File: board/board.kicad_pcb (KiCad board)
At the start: 2 copper layers, 21 x 13 mm, 16 parts, among them J1 013_PoE_rectified, J2 014_PoE_controlled, Q1 PSMN5R2-60YL, U1 LT4275AIDDPBF-LT4275AIDDPBF

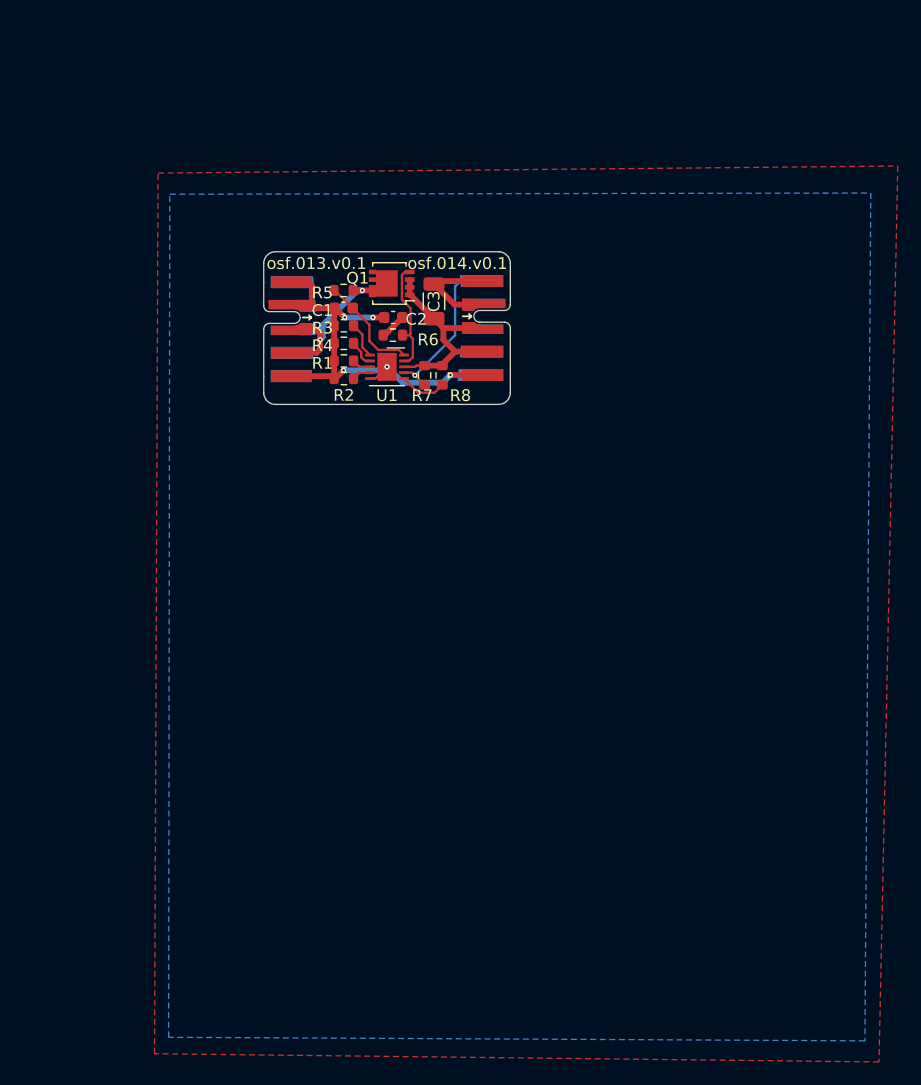
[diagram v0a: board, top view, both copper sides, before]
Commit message: changed PSMN5R2 footprint from LFPAK33 to LFPAK56
The PSMN5R2 is not available in LFPAK33.
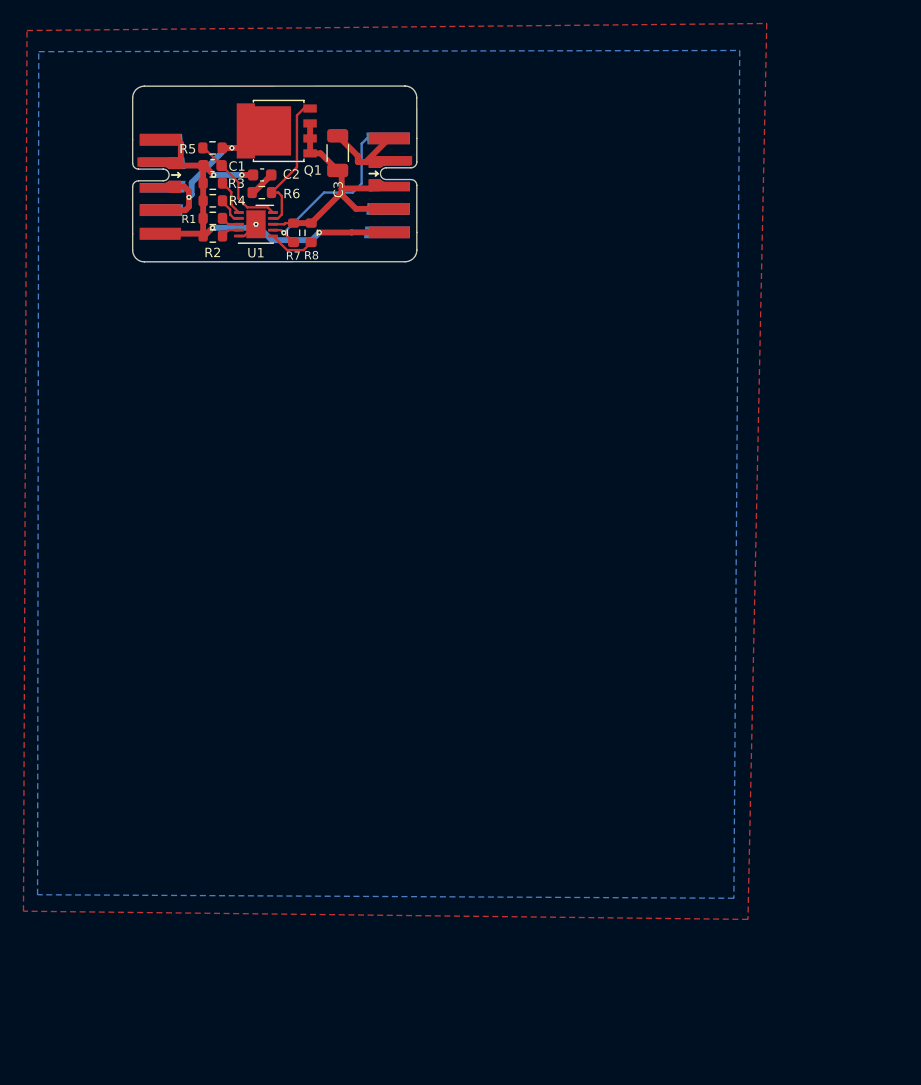
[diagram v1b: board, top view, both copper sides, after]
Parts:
- Q1: footprint Package_TO_SOT_SMD:LFPAK33 -> Package_TO_SOT_SMD:LFPAK56
- moved C2 16.5 mm to (76.9, 67.5)
- moved C1 16.5 mm to (72.6, 66.7)
- moved J1 16.5 mm to (65.8, 68.5)
- moved LOGO1 16.5 mm to (76.3, 68.9)
- moved R1 16.5 mm to (72.7, 71.2)
- moved R2 16.5 mm to (72.7, 72.7)
- moved R3 16.5 mm to (72.7, 68.2)
- moved R4 16.5 mm to (72.7, 69.7)
- moved R5 16.5 mm to (72.6, 65.2)
- moved R6 16.5 mm to (76.8, 69.0)
- moved R7 16.5 mm to (79.5, 72.4)
- moved R8 16.5 mm to (81.0, 72.4)
- moved U1 16.5 mm to (76.3, 71.7)
- moved Q1 16.3 mm to (78.1, 63.7)
- moved C3 15.1 mm to (83.3, 65.6)
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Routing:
- net /implementation/poe+_out: track 17.1 -> 22.5 mm
- net GND: track 44.2 -> 48.9 mm
- net /implementation/PG: track 13.7 -> 16.4 mm
- net Net-(Q1-Pad4): track 9.70 -> 12.3 mm
- net /implementation/poe+_in: track 15.1 -> 16.9 mm
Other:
- board size 21 x 13 mm -> 24.2 x 15 mm
- board text added: "osf.b027.v0.2"
- board text removed: "osf.013.v0.1"
- board text removed: "osf.014.v0.1"
- board text removed: "osf.b027.v0.1"

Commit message: Moved Q1 from front to back
Q1 from front to back and keeped the size of pcb
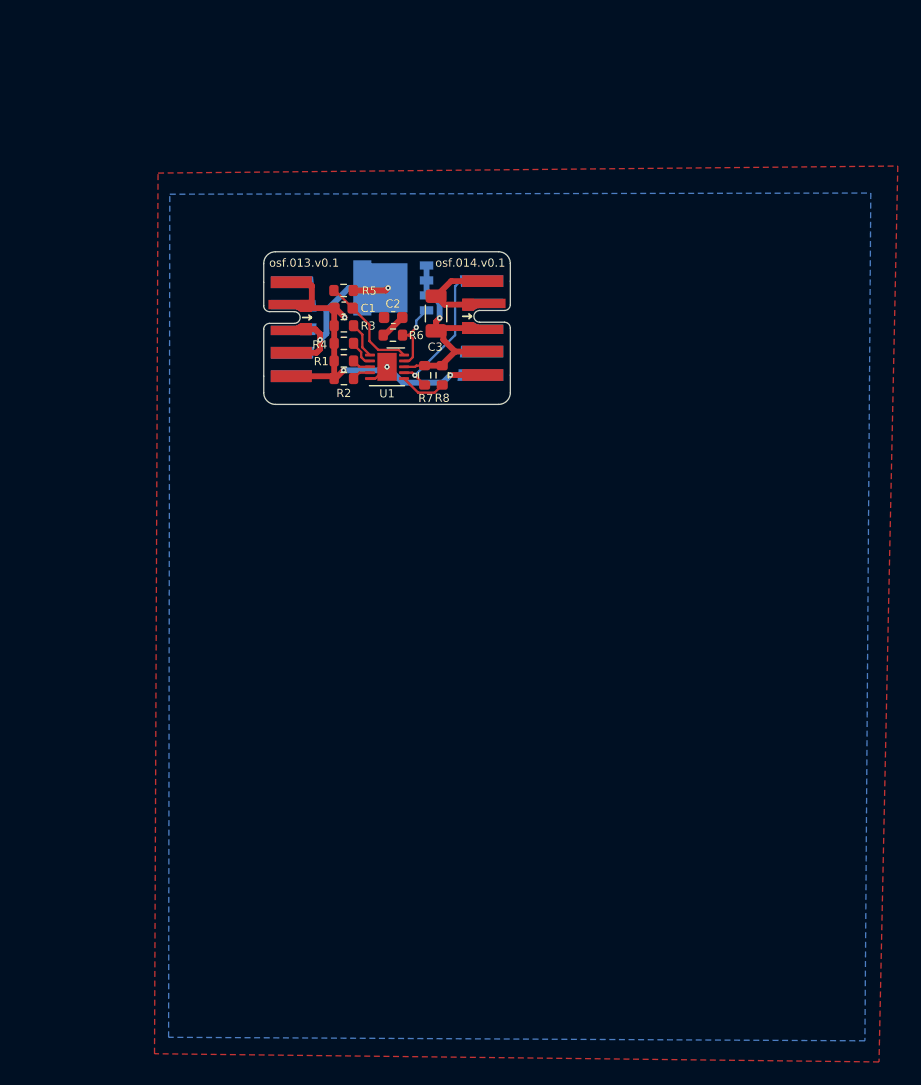
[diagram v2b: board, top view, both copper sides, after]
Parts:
- removed LOGO1: Logo_Open_Hardware_Small, Symbol:OSHW-Symbol_6.7x6mm_SilkScreen
- Q1: moved to B.Cu
- moved Q1 16.6 mm to (88.0, 77.1)
- moved C2 16.5 mm to (88.0, 79.6)
- moved C1 16.5 mm to (83.8, 78.8)
- moved J1 16.5 mm to (77.0, 80.6)
- moved R1 16.5 mm to (83.8, 83.3)
- moved R2 16.5 mm to (83.8, 84.8)
- moved R3 16.5 mm to (83.8, 80.3)
- moved R4 16.5 mm to (83.8, 81.8)
- moved R5 16.5 mm to (83.8, 77.3)
- moved R6 16.5 mm to (88.0, 81.1)
- moved R7 16.5 mm to (90.7, 84.5)
- moved R8 16.5 mm to (92.2, 84.5)
- moved U1 16.5 mm to (87.5, 83.8)
- moved C3 16.0 mm to (91.7, 79.3)
- moved J2 14.5 mm to (98.0, 80.5)
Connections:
- net /implementation/PG renamed /Controller/PG
- net /implementation/poe+_in renamed /Controller/poe+_in
- net /implementation/poe+_out renamed /Controller/poe+_out
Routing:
- net GND: track 48.9 -> 40.5 mm, vias 5 -> 4
- net Net-(Q1-Pad4): track 12.3 -> 6.72 mm, vias 0 -> 1
- net /Controller/poe+_out: track 22.5 -> 18.9 mm, vias 0 -> 1
- net /Controller/PG: track 16.4 -> 13.7 mm
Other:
- board size 24.2 x 15 mm -> 21 x 13 mm
- board text added: "osf.013.v0.1"
- board text added: "osf.014.v0.1"

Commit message: updated connectors
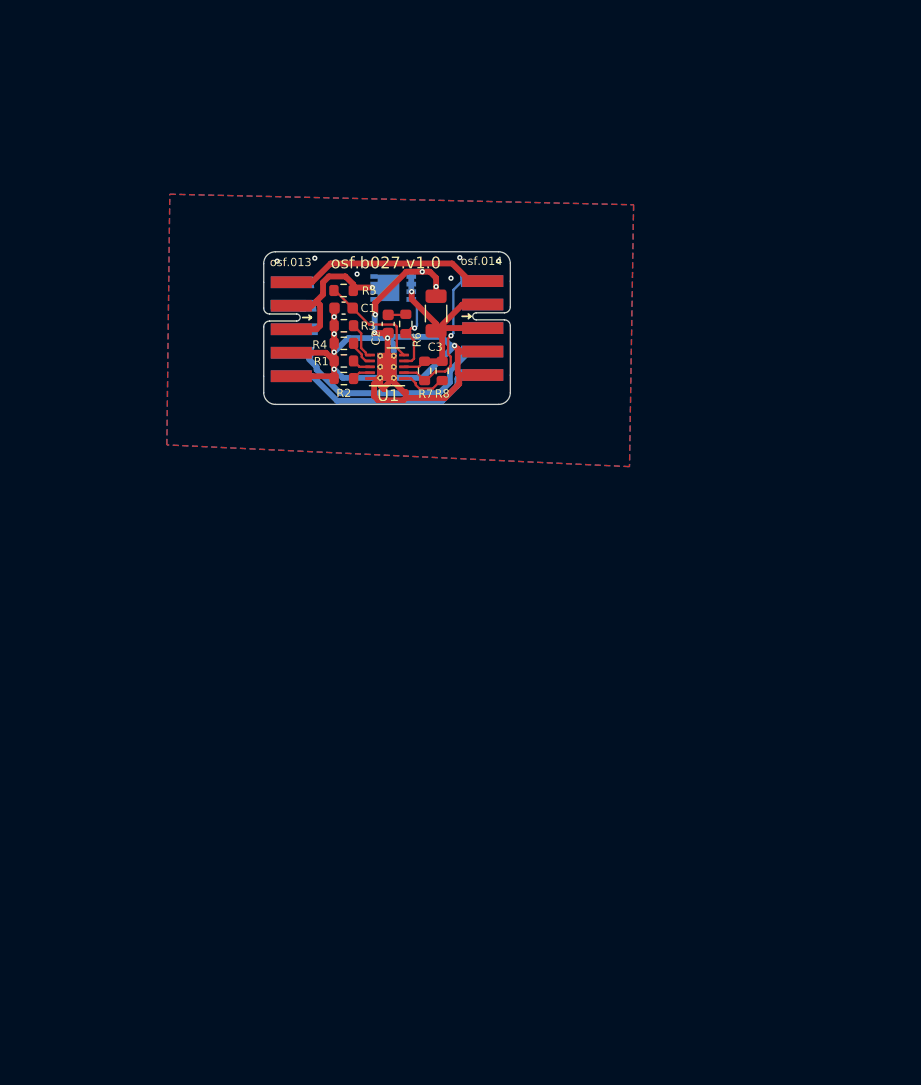
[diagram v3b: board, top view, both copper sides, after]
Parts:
- Q1: value PSMN5R2-60YL -> PSMN040-100MSEX; footprint Package_TO_SOT_SMD:LFPAK56 -> Package_TO_SOT_SMD:LFPAK33
- U1: value LT4275AIDDPBF-LT4275AIDDPBF -> LT4275AIDDPBF; footprint Package_DFN_QFN:DFN-10-1EP_3x3mm_P0.5mm_EP1.65x2.38mm -> Package_DFN_QFN:DFN-10-1EP_3x3mm_P0.5mm_EP1.65x2.38mm_ThermalVias
- moved R6 1.45 mm to (89.1, 80.2), turned to 90 degrees
- moved C2 0.70 mm to (87.6, 80.2), turned to -90 degrees
- moved R7 0.38 mm to (90.7, 84.2)
- moved R8 0.38 mm to (92.2, 84.2)
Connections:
- net Net-(R1-Pad1) renamed /Controller/RCLASS
- net Net-(R2-Pad1) renamed /Controller/RCLASS++
- net Net-(R3-Pad1) renamed /Controller/IEEEULVO
- net Net-(R4-Pad1) renamed /Controller/AUX
- C1 pad 2: GND -> /Controller/PoE-
- C2 pad 2: GND -> /Controller/PoE-
- C3 pad 2: GND -> /Controller/PoE-
- J1 pad 10: (no net) -> Net-(J1-Pad10)
- J1 pad 2: GND -> /Controller/poe+_in
- J1 pad 4: /Controller/poe+_in -> /Controller/PoE-
- J1 pad 5: GND -> /Controller/PoE-
- J1 pad 9: (no net) -> Net-(J1-Pad9)
- J2 pad 10: (no net) -> Net-(J1-Pad10)
- J2 pad 2: GND -> /Controller/poe+_out
- J2 pad 4: /Controller/poe+_out -> /Controller/PoE-
- J2 pad 5: GND -> /Controller/PoE-
- J2 pad 9: (no net) -> Net-(J1-Pad9)
- R1 pad 2: GND -> /Controller/PoE-
- R2 pad 2: GND -> /Controller/PoE-
- R3 pad 2: GND -> /Controller/PoE-
- R4 pad 2: GND -> /Controller/PoE-
- U1 pad 11: GND -> /Controller/PoE-
- U1 pad 5: GND -> /Controller/PoE-
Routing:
- net /Controller/PoE-: track 0.00 -> 77.9 mm, vias 0 -> 16
- net GND: track 40.5 -> 17.6 mm, vias 4 -> 0
- net Net-(J1-Pad10): track 0.00 -> 18.3 mm
- net Net-(J1-Pad9): track 0.00 -> 18.1 mm
- net /Controller/poe+_out: track 18.9 -> 20.7 mm
- net /Controller/poe+_in: track 17.1 -> 15.6 mm, vias 2 -> 1
- net Net-(C2-Pad1): track 2.25 -> 1.52 mm
- net /Controller/PG: track 13.7 -> 14.3 mm
- added copper zone on B.Cu, net /Controller/PoE-
- added copper zone on F.Cu, net /Controller/PoE-
- removed copper zone on B.Cu, net GND
- removed copper zone on F.Cu, net GND
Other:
- board text added: "osf.013"
- board text added: "osf.014"
- board text added: "osf.b027.v1.0"
- board text removed: "osf.013.v0.1"
- board text removed: "osf.014.v0.1"
- board text removed: "osf.b027.v0.2"

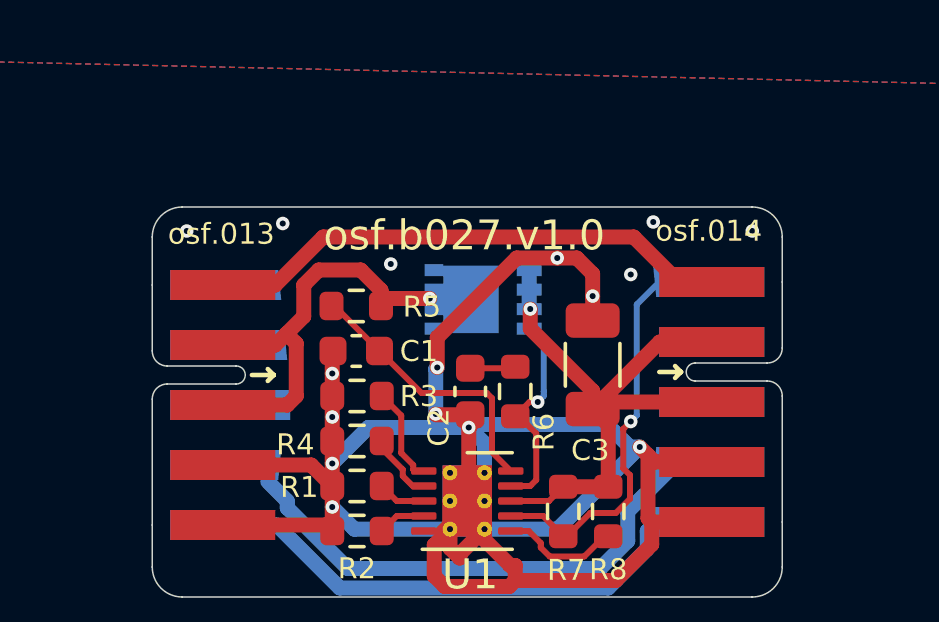
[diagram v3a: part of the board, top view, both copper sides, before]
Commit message: added power doo cinnection upstream
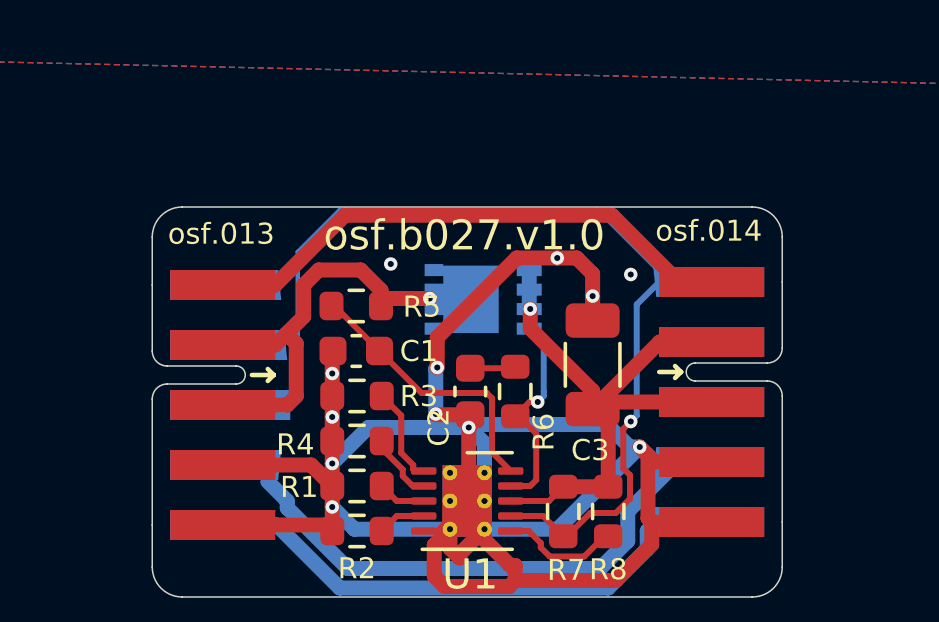
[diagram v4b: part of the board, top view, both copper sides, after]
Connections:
- J1 pad 8: (no net) -> /Controller/PG
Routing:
- net /Controller/PG: track 14.3 -> 36.7 mm
- net GND: track 17.6 -> 18.2 mm
- net /Controller/PoE-: vias 16 -> 12
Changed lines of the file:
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@@
   (net 8 "Net-(J1-Pad9)")
   (net 9 "Net-(J1-Pad10)")
-  (net 10 "Net-(U1-Pad9)")
-  (net 11 "Net-(U1-Pad6)")
+  (net 10 "Net-(Q1-Pad4)")
+  (net 11 "Net-(R8-Pad2)")
   (net 12 "/Controller/RCLASS")
   (net 13 "/Controller/RCLASS++")
@@
       (net 7 "/Controller/PoE-") (pinfunction "GND") (pintype "power_in"))
     (pad "6" smd roundrect (at 1.45 1) (size 0.85 0.25) (layers "F.Cu" "F.Paste" "F.Mask") (roundrect_rratio 0.25)
-      (net 11 "Net-(U1-Pad6)") (pinfunction "*T2P/NC") (pintype "passive"))
+      (net 11 "Net-(R8-Pad2)") (pinfunction "*T2P/NC") (pintype "passive"))
     (pad "7" smd roundrect (at 1.45 0.5) (size 0.85 0.25) (layers "F.Cu" "F.Paste" "F.Mask") (roundrect_rratio 0.25)
       (net 4 "/Controller/PG") (pinfunction "PWRGD") (pintype "passive"))
@@
       (net 3 "/Controller/poe+_out") (pinfunction "HSSRC") (pintype "passive"))
     (pad "9" smd roundrect (at 1.45 -0.5) (size 0.85 0.25) (layers "F.Cu" "F.Paste" "F.Mask") (roundrect_rratio 0.25)
-      (net 10 "Net-(U1-Pad9)") (pinfunction "HSGATE") (pintype "passive"))
+      (net 10 "Net-(Q1-Pad4)") (pinfunction "HSGATE") (pintype "passive"))
     (pad "10" smd roundrect (at 1.45 -1) (size 0.85 0.25) (layers "F.Cu" "F.Paste" "F.Mask") (roundrect_rratio 0.25)
       (net 5 "Net-(C1-Pad1)") (pinfunction "VPORT") (pintype "passive"))
@@
       ))
     (pad "8" smd rect (at 0 -2.6 270) (size 1 4) (layers "B.Cu" "B.Mask")
-      (zone_connect 0))
+      (net 4 "/Controller/PG") (pinfunction "PWRGOOD") (pintype "bidirectional") (zone_connect 0))
     (pad "9" smd custom (at 2 -2.4 270) (size 1 3.6) (layers "B.Cu" "B.Mask")
       (net 8 "Net-(J1-Pad9)") (pinfunction "3.3V") (pintype "power_in") (zone_connect 0)
@@
     (fp_line (start -0.8 0.4125) (end -0.8 -0.4125) (layer "F.Fab") (width 0.1))
     (pad "1" smd roundrect (at -0.825 0 90) (size 0.8 0.95) (layers "F.Cu" "F.Paste" "F.Mask") (roundrect_rratio 0.25)
-      (net 10 "Net-(U1-Pad9)") (pintype "passive"))
+      (net 10 "Net-(Q1-Pad4)") (pintype "passive"))
     (pad "2" smd roundrect (at 0.825 0 90) (size 0.8 0.95) (layers "F.Cu" "F.Paste" "F.Mask") (roundrect_rratio 0.25)
       (net 6 "Net-(C2-Pad1)") (pintype "passive"))
@@
       (net 3 "/Controller/poe+_out") (pintype "passive"))
     (pad "2" smd roundrect (at 0.825 0 270) (size 0.8 0.95) (layers "F.Cu" "F.Paste" "F.Mask") (roundrect_rratio 0.25)
-      (net 11 "Net-(U1-Pad6)") (pintype "passive"))
+      (net 11 "Net-(R8-Pad2)") (pintype "passive"))
     (model "${KICAD6_3DMODEL_DIR}/Resistor_SMD.3dshapes/R_0603_1608Metric.wrl"
       (offset (xyz 0 0 0))
@@
       (net 3 "/Controller/poe+_out") (pinfunction "S") (pintype "passive"))
     (pad "4" smd rect (at -1.535 -0.975 180) (size 0.83 0.4) (layers "B.Cu" "B.Mask")
-      (net 10 "Net-(U1-Pad9)") (pinfunction "G") (pintype "passive"))
+      (net 10 "Net-(Q1-Pad4)") (pinfunction "G") (pintype "passive"))
     (pad "5" smd custom (at 0.405 0 180) (size 1.85 2.25) (layers "B.Cu" "B.Mask")
       (net 2 "/Controller/poe+_in") (pinfunction "D") (pintype "passive") (zone_connect 2)
@@
     (effects (font (size 0.7 0.7) (thickness 0.15)))
   )
-  (segment (start 81.1 76.6) (end 82.7 75) (width 0.5) (layer "F.Cu") (net 1))
+  (segment (start 79.35 76.6) (end 81.1 76.6) (width 0.5) (layer "F.Cu") (net 1))
+  (segment (start 92.325 74.275) (end 94.55 76.5) (width 0.5) (layer "F.Cu") (net 1))
+  (segment (start 83.425 74.275) (end 92.325 74.275) (width 0.5) (layer "F.Cu") (net 1))
   (segment (start 94.55 76.5) (end 95.65 76.5) (width 0.5) (layer "F.Cu") (net 1))
-  (segment (start 79.35 76.6) (end 81.1 76.6) (width 0.5) (layer "F.Cu") (net 1))
-  (segment (start 82.7 75) (end 93.05 75) (width 0.5) (layer "F.Cu") (net 1))
-  (segment (start 93.05 75) (end 94.55 76.5) (width 0.5) (layer "F.Cu") (net 1))
+  (segment (start 81.1 76.6) (end 83.425 74.275) (width 0.5) (layer "F.Cu") (net 1))
   (segment (start 79.35 80.6) (end 81.5 80.6) (width 0.5) (layer "F.Cu") (net 2))
   (segment (start 82.05 77.65) (end 82.05 76.6) (width 0.5) (layer "F.Cu") (net 2))
@@
   (segment (start 90.025 84.3) (end 90.7 84.975) (width 0.2) (layer "F.Cu") (net 4))
   (via (at 92.95 81.15) (size 0.45) (drill 0.2) (layers "F.Cu" "B.Cu") (net 4))
+  (segment (start 81.85 80.15) (end 81.85 75.5) (width 0.15) (layer "B.Cu") (net 4))
+  (segment (start 94.25 76.5) (end 95.6 76.5) (width 0.15) (layer "B.Cu") (net 4))
+  (segment (start 91.85 74.1) (end 94.25 76.5) (width 0.15) (layer "B.Cu") (net 4))
   (segment (start 93.15 80.95) (end 93.15 77.25) (width 0.2) (layer "B.Cu") (net 4))
+  (segment (start 83.25 74.1) (end 91.85 74.1) (width 0.15) (layer "B.Cu") (net 4))
   (segment (start 93.15 77.25) (end 93.9 76.5) (width 0.2) (layer "B.Cu") (net 4))
+  (segment (start 79.6 80.6) (end 81.4 80.6) (width 0.15) (layer "B.Cu") (net 4))
+  (segment (start 81.4 80.6) (end 81.85 80.15) (width 0.15) (layer "B.Cu") (net 4))
+  (segment (start 81.85 75.5) (end 83.25 74.1) (width 0.15) (layer "B.Cu") (net 4))
   (segment (start 93.9 76.5) (end 95.6 76.5) (width 0.2) (layer "B.Cu") (net 4))
   (segment (start 92.95 81.15) (end 93.15 80.95) (width 0.2) (layer "B.Cu") (net 4))
@@
   (segment (start 87.55 83.75) (end 87.5 83.8) (width 0.5) (layer "F.Cu") (net 7))
   (via (at 93.25 82) (size 0.45) (drill 0.2) (layers "F.Cu" "B.Cu") (net 7))
-  (via (at 78.15 74.8) (size 0.45) (drill 0.2) (layers "F.Cu" "B.Cu") (free) (net 7))
   (via (at 87.55 81.35) (size 0.45) (drill 0.2) (layers "F.Cu" "B.Cu") (net 7))
   (via (at 91.68 76.97) (size 0.45) (drill 0.2) (layers "F.Cu" "B.Cu") (net 7))
@@
   (via (at 83 79.55) (size 0.45) (drill 0.2) (layers "F.Cu" "B.Cu") (net 7))
   (via (at 86.5 79.35) (size 0.45) (drill 0.2) (layers "F.Cu" "B.Cu") (net 7))
-  (via (at 97 74.8) (size 0.45) (drill 0.2) (layers "F.Cu" "B.Cu") (free) (net 7))
-  (via (at 93.7 74.5) (size 0.45) (drill 0.2) (layers "F.Cu" "B.Cu") (free) (net 7))
   (via (at 86.45 80.9) (size 0.45) (drill 0.2) (layers "F.Cu" "B.Cu") (net 7))
-  (via (at 81.35 74.55) (size 0.45) (drill 0.2) (layers "F.Cu" "B.Cu") (free) (net 7))
   (via (at 92.95 76.25) (size 0.45) (drill 0.2) (layers "F.Cu" "B.Cu") (free) (net 7))
   (via (at 83 81) (size 0.45) (drill 0.2) (layers "F.Cu" "B.Cu") (net 7))
